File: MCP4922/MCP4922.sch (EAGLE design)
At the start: 27 parts, among them U1 MCP4922, U2 MCP4922, U3 LM4040D50IDBZR

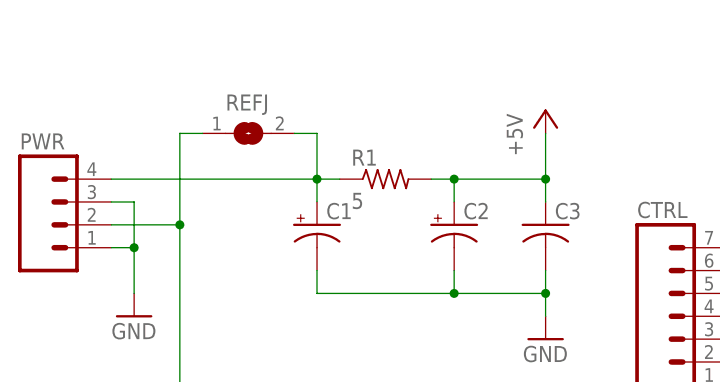
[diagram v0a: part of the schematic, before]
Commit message: Added jumper for voltage reference; readme
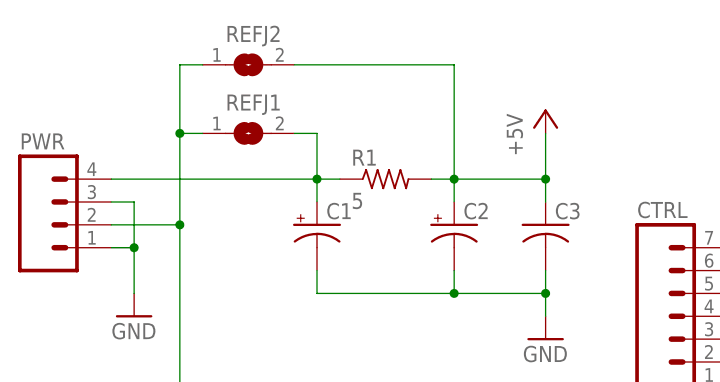
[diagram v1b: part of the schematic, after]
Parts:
- added REFJ2: (no value), jumper:SJ
- renumbered REFJ to REFJ1
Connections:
- net +5V: now also REFJ2.2
- net N$10: now also REFJ2.1
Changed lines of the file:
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@@
 <setting verticaltext="up"/>
 </settings>
-<grid distance="0.1" unitdist="inch" unit="inch" style="lines" multiple="1" display="yes" altdistance="0.01" altunitdist="inch" altunit="inch"/>
+<grid distance="0.1" unitdist="inch" unit="inch" style="lines" multiple="1" display="no" altdistance="0.01" altunitdist="inch" altunit="inch"/>
 <layers>
 <layer number="1" name="Top" color="4" fill="1" visible="no" active="no"/>
@@
 <part name="JP3" library="SparkFun-Connectors" deviceset="M02" device="LOCK"/>
 <part name="JP4" library="SparkFun-Connectors" deviceset="M02" device="LOCK"/>
-<part name="REFJ" library="jumper" deviceset="SJ" device=""/>
+<part name="REFJ1" library="jumper" deviceset="SJ" device=""/>
 <part name="CTRL" library="SparkFun-Connectors" deviceset="M07" device="LOCK"/>
+<part name="REFJ2" library="jumper" deviceset="SJ" device=""/>
 </parts>
 <sheets>
@@
 <instance part="JP3" gate="G$1" x="132.08" y="25.4" rot="R180"/>
 <instance part="JP4" gate="G$1" x="132.08" y="12.7" rot="R180"/>
-<instance part="REFJ" gate="1" x="-33.02" y="88.9"/>
+<instance part="REFJ1" gate="1" x="-33.02" y="88.9"/>
 <instance part="CTRL" gate="G$1" x="15.24" y="66.04"/>
+<instance part="REFJ2" gate="1" x="-33.02" y="96.52"/>
 </instances>
 <busses>
@@
 <wire x1="0" y1="88.9" x2="0" y2="83.82" width="0.1524" layer="91"/>
 <junction x="0" y="83.82"/>
+<pinref part="REFJ2" gate="1" pin="2"/>
+<wire x1="-27.94" y1="96.52" x2="-10.16" y2="96.52" width="0.1524" layer="91"/>
+<wire x1="-10.16" y1="96.52" x2="-10.16" y2="83.82" width="0.1524" layer="91"/>
 </segment>
 </net>
@@
 <wire x1="-25.4" y1="83.82" x2="-25.4" y2="81.28" width="0.1524" layer="91"/>
 <junction x="-25.4" y="83.82"/>
-<pinref part="REFJ" gate="1" pin="2"/>
+<pinref part="REFJ1" gate="1" pin="2"/>
 <wire x1="-27.94" y1="88.9" x2="-25.4" y2="88.9" width="0.1524" layer="91"/>
 <wire x1="-25.4" y1="88.9" x2="-25.4" y2="83.82" width="0.1524" layer="91"/>
@@
 <wire x1="-40.64" y1="78.74" x2="-40.64" y2="53.34" width="0.1524" layer="91"/>
 <wire x1="-40.64" y1="53.34" x2="-35.56" y2="53.34" width="0.1524" layer="91"/>
-<pinref part="REFJ" gate="1" pin="1"/>
+<pinref part="REFJ1" gate="1" pin="1"/>
 <wire x1="-38.1" y1="88.9" x2="-40.64" y2="88.9" width="0.1524" layer="91"/>
 <wire x1="-40.64" y1="88.9" x2="-40.64" y2="78.74" width="0.1524" layer="91"/>
 <junction x="-40.64" y="78.74"/>
-</segment>
-</net>
+<pinref part="REFJ2" gate="1" pin="1"/>
+<wire x1="-38.1" y1="96.52" x2="-40.64" y2="96.52" width="0.1524" layer="91"/>
+<wire x1="-40.64" y1="96.52" x2="-40.64" y2="88.9" width="0.1524" layer="91"/>
+<junction x="-40.64" y="88.9"/>
+</segment>
+</net>
